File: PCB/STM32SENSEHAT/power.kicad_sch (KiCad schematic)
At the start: 30 parts, among them IC1 DW01A, J1 USB_B_Micro, J7 Conn_01x05_Pin, Q1 NMOS, Q2 NMOS, U1 MCP1700x-330xxTT, U2 TP4056, U3 FT230XQ

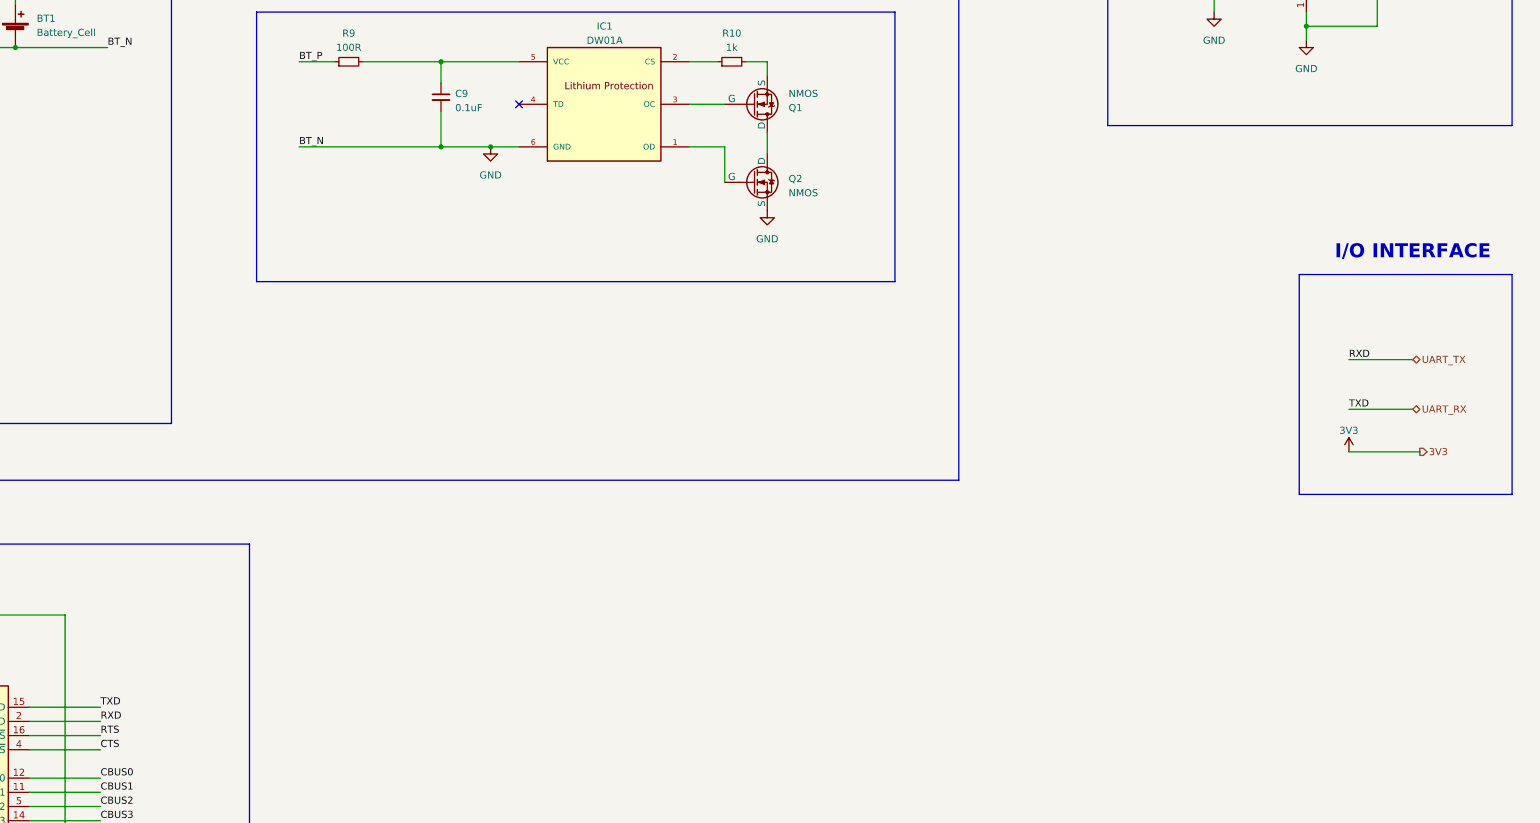
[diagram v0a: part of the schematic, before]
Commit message: Removed the extra sensor, Modified BME280 interfacing and FTDI UART pins. Added Manual Reset to MCU and configured BOOT pin
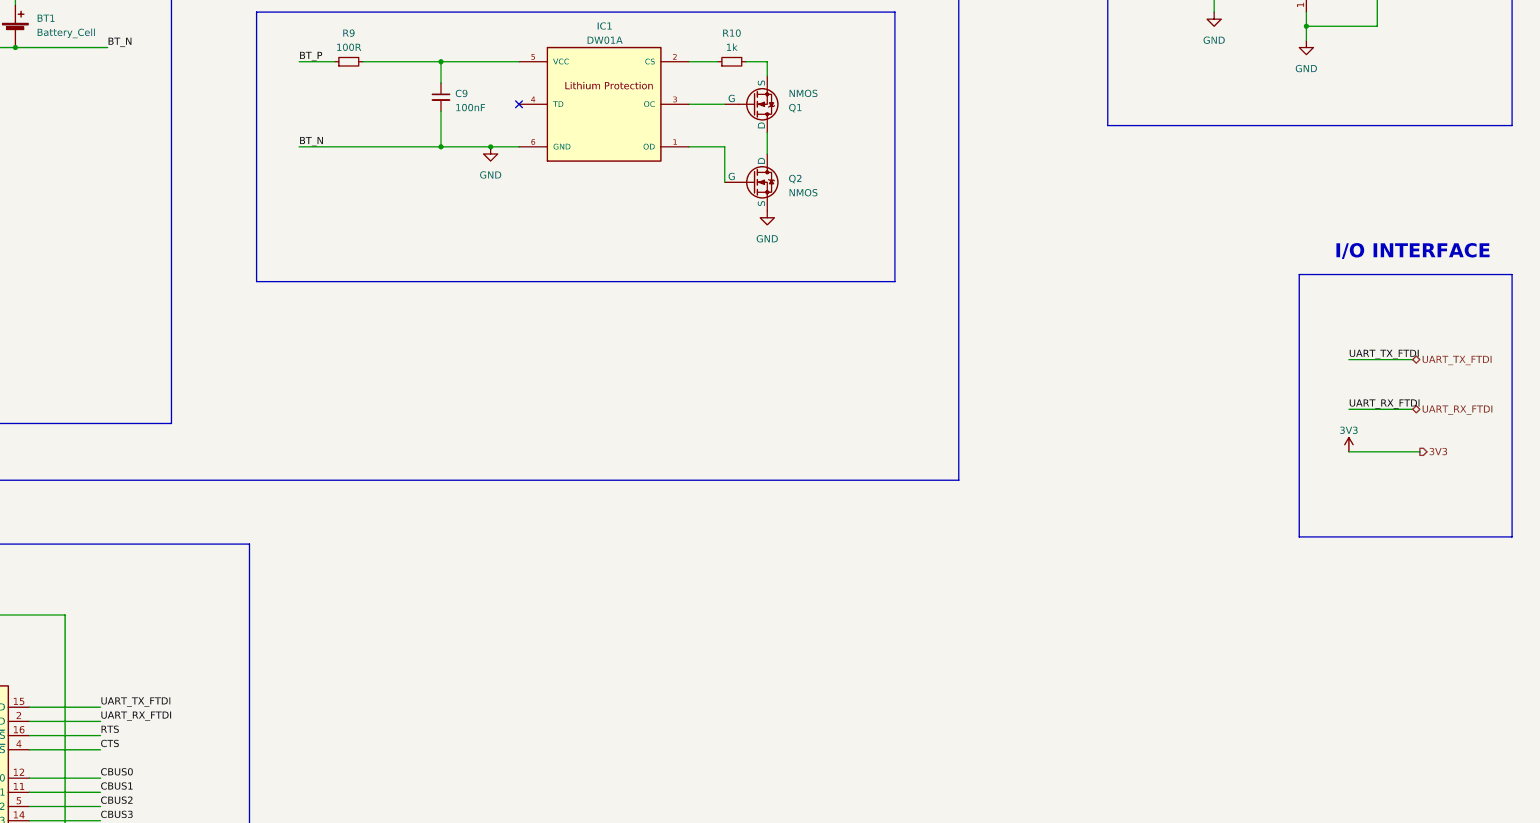
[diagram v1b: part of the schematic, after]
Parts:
- C9: value 0.1uF -> 100nF
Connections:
- net UART_RX renamed UART_TX_FTDI
- net UART_TX renamed UART_RX_FTDI
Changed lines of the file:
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@@
     (fill (type none))
   )
-  (rectangle (start 359.41 101.6) (end 397.51 140.97)
+  (rectangle (start 359.41 101.6) (end 397.51 148.59)
     (stroke (width 0) (type default))
     (fill (type none))
@@
     (effects (font (size 1.27 1.27)) (justify left bottom))
   )
-  (label "TXD" (at 368.3 125.73 0) (fields_autoplaced)
-    (effects (font (size 1.27 1.27)) (justify left bottom))
-  )
   (label "BT_N" (at 180.34 78.74 0) (fields_autoplaced)
     (effects (font (size 1.27 1.27)) (justify left bottom))
   )
+  (label "UART_RX_FTDI" (at 368.3 125.73 0) (fields_autoplaced)
+    (effects (font (size 1.27 1.27)) (justify left bottom))
+  )
   (label "D-" (at 50.8 189.23 0) (fields_autoplaced)
     (effects (font (size 1.27 1.27)) (justify left bottom))
@@
     (effects (font (size 1.27 1.27)) (justify left bottom))
   )
+  (label "UART_TX_FTDI" (at 144.78 179.07 0) (fields_autoplaced)
+    (effects (font (size 1.27 1.27)) (justify left bottom))
+  )
   (label "BT_P" (at 180.34 63.5 0) (fields_autoplaced)
     (effects (font (size 1.27 1.27)) (justify left bottom))
@@
     (effects (font (size 1.27 1.27)) (justify left bottom))
   )
-  (label "RXD" (at 144.78 181.61 0) (fields_autoplaced)
-    (effects (font (size 1.27 1.27)) (justify left bottom))
-  )
   (label "D-" (at 97.79 240.03 0) (fields_autoplaced)
     (effects (font (size 1.27 1.27)) (justify left bottom))
@@
     (effects (font (size 1.27 1.27)) (justify left bottom))
   )
+  (label "UART_RX_FTDI" (at 144.78 181.61 0) (fields_autoplaced)
+    (effects (font (size 1.27 1.27)) (justify left bottom))
+  )
   (label "BT_P" (at 335.28 46.99 0) (fields_autoplaced)
     (effects (font (size 1.27 1.27)) (justify left bottom))
@@
     (effects (font (size 1.27 1.27)) (justify left bottom))
   )
-  (label "TXD" (at 144.78 179.07 0) (fields_autoplaced)
+  (label "UART_TX_FTDI" (at 368.3 116.84 0) (fields_autoplaced)
     (effects (font (size 1.27 1.27)) (justify left bottom))
   )
@@
   )
   (label "VBUS" (at 50.8 181.61 0) (fields_autoplaced)
-    (effects (font (size 1.27 1.27)) (justify left bottom))
-  )
-  (label "RXD" (at 368.3 116.84 0) (fields_autoplaced)
     (effects (font (size 1.27 1.27)) (justify left bottom))
   )
@@
     (effects (font (size 1.27 1.27)) (justify left))
   )
-  (hierarchical_label "UART_TX" (shape bidirectional) (at 379.73 116.84 0) (fields_autoplaced)
+  (hierarchical_label "UART_TX_FTDI" (shape bidirectional) (at 379.73 116.84 0) (fields_autoplaced)
     (effects (font (size 1.27 1.27)) (justify left))
   )
-  (hierarchical_label "UART_RX" (shape bidirectional) (at 379.73 125.73 0) (fields_autoplaced)
+  (hierarchical_label "UART_RX_FTDI" (shape bidirectional) (at 379.73 125.73 0) (fields_autoplaced)
     (effects (font (size 1.27 1.27)) (justify left))
   )
@@
       (effects (font (size 1.27 1.27)) (justify left))
     )
-    (property "Value" "0.1uF" (at 208.28 71.7613 0)
-      (effects (font (size 1.27 1.27)) (justify left))
-    )
+    (property "Value" "100nF" (at 208.28 71.7613 0)
+      (effects (font (size 1.27 1.27)) (justify left))
+    )

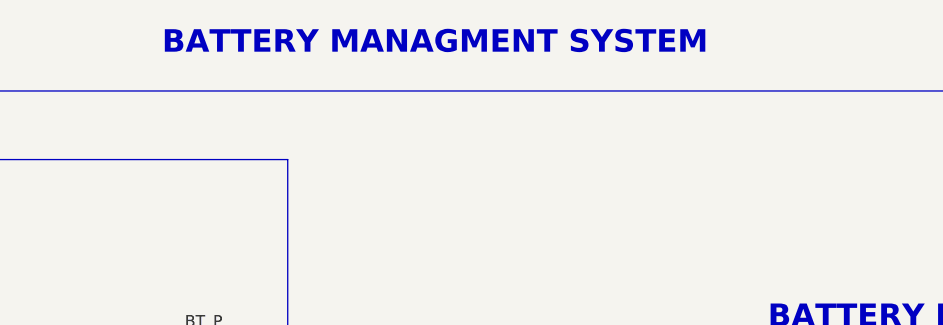
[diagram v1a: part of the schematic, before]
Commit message: Add STM32SENSEHAT, power, sensor, and mcu schematic file
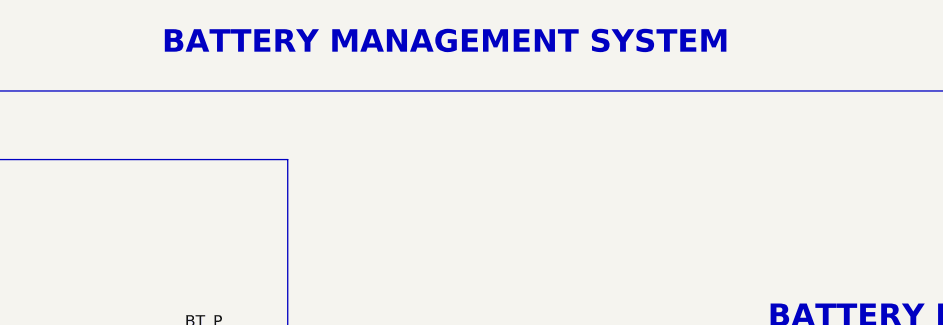
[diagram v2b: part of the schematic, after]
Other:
- note added: "BATTERY MANAGEMENT SYSTEM"
- note removed: "BATTERY MANAGMENT SYSTEM"
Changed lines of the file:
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@@
     (effects (font (size 2.5 2.5) (thickness 0.5) bold) (justify left bottom))
   )
-  (text "BATTERY MANAGMENT SYSTEM\n" (at 143.51 20.32 0)
+  (text "BATTERY MANAGEMENT SYSTEM\n" (at 143.51 20.32 0)
     (effects (font (size 2.5 2.5) (thickness 0.5) bold) (justify left bottom))
   )

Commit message: Revised schematics. Moved USB and EEPROM sub modules to MCU sheet and and rectified the top sheet accordingly
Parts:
- removed C1, C2: 47pF, symbol Device:C_Small
- removed C3: 10nF, symbol Device:C_Small
- removed C4, C5: 100nF, symbol Device:C_Small
- removed C6: 4.7uF, symbol Device:C_Small
- removed FB1: FerriteBead, symbol Device:FerriteBead
- removed J1: USB_B_Micro, symbol Connector:USB_B_Micro
- removed J7: Conn_01x05_Pin, symbol Connector:Conn_01x05_Pin
- removed R2, R3: 27R, symbol Device:R_Small
- removed U3: FT230XQ, Package_DFN_QFN:QFN-16-1EP_4x4mm_P0.65mm_EP2.1x2.1mm, symbol Interface_USB:FT230XQ
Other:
- note removed: "USB-FTDI INTERFACE"

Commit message: Added Battery Volatge Sesnsing capability
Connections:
- net BT_P renamed BAT_VOLTAGE
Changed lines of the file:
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@@
     (stroke (width 0) (type default))
   )
-  (wire (pts (xy 368.3 133.35) (xy 381 133.35))
+  (wire (pts (xy 350.52 123.19) (xy 363.22 123.19))
     (stroke (width 0) (type default))
   )
@@
     (stroke (width 0) (type default))
   )
+  (wire (pts (xy 350.52 107.95) (xy 363.22 107.95))
+    (stroke (width 0) (type default))
+  )
   (wire (pts (xy 82.55 104.14) (xy 82.55 96.52))
     (stroke (width 0) (type default))
@@
     (fill (type none))
   )
-  (rectangle (start 359.41 101.6) (end 397.51 148.59)
+  (rectangle (start 341.63 91.44) (end 379.73 138.43)
     (stroke (width 0) (type default))
     (fill (type none))
@@
     (effects (font (size 2.5 2.5) (thickness 0.5) bold) (justify left bottom))
   )
-  (text "I/O INTERFACE" (at 365.76 99.06 0)
+  (text "I/O INTERFACE" (at 347.98 88.9 0)
     (effects (font (size 2.5 2.5) (thickness 0.5) bold) (justify left bottom))
   )
@@
     (effects (font (size 1.27 1.27)) (justify left bottom))
   )
+  (label "BT_P" (at 350.52 107.95 0) (fields_autoplaced)
+    (effects (font (size 1.27 1.27)) (justify left bottom))
+  )
   (hierarchical_label "5V_USB" (shape input) (at 101.6 43.18 0) (fields_autoplaced)
     (effects (font (size 1.27 1.27)) (justify left))
   )
-  (hierarchical_label "3V3" (shape output) (at 381 133.35 0) (fields_autoplaced)
+  (hierarchical_label "3V3" (shape output) (at 363.22 123.19 0) (fields_autoplaced)
+    (effects (font (size 1.27 1.27)) (justify left))
+  )
+  (hierarchical_label "BAT_VOLTAGE" (shape input) (at 363.22 107.95 0) (fields_autoplaced)
     (effects (font (size 1.27 1.27)) (justify left))
   )
@@
     )
   )
-  (symbol (lib_id "power:VCC") (at 368.3 133.35 0) (unit 1)
-    (in_bom yes) (on_board yes) (dnp no) (fields_autoplaced)
-    (property "Reference" "#PWR052" (at 368.3 137.16 0)
-      (effects (font (size 1.27 1.27)) hide)
-    )
-    (property "Value" "3V3" (at 368.3 129.54 0)
+  (symbol (lib_id "power:VCC") (at 350.52 123.19 0) (unit 1)
+    (in_bom yes) (on_board yes) (dnp no) (fields_autoplaced)
+    (property "Reference" "#PWR052" (at 350.52 127 0)
+      (effects (font (size 1.27 1.27)) hide)
+    )
+    (property "Value" "3V3" (at 350.52 119.38 0)
       (effects (font (size 1.27 1.27) (color 132 0 0 1)))
     )
-    (property "Footprint" "" (at 368.3 133.35 0)
-      (effects (font (size 1.27 1.27)) hide)
-    )
-    (property "Datasheet" "" (at 368.3 133.35 0)
-      (effects (font (size 1.27 1.27)) hide)
-    )
+    (property "Footprint" "" (at 350.52 123.19 0)
+      (effects (font (size 1.27 1.27)) hide)
+    )
+    (property "Datasheet" "" (at 350.52 123.19 0)
+      (effects (font (size 1.27 1.27)) hide)
+    )

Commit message: Protectuion features added to all schematica
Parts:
- removed Q1, Q2: NMOS, symbol Simulation_SPICE:NMOS
- added C15, C16, C17: 1uF, symbol Device:C_Small
- added D3: D_Schottky, symbol Device:D_Schottky
- added Q1: AO3401A, Package_TO_SOT_SMD:SOT-23, symbol Transistor_FET:AO3401A
- added R19 (x4): 0R, symbol Device:R_Small
- added R35: 10k, symbol Device:R_Small
- added TP5, TP6: TestPoint, symbol Connector:TestPoint
- added U7: 8205A, TSSOP8, symbol 8205A:8205A
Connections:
- net BAT_VOLTAGE: now also Q1.3 (D); no longer C10.1, U1.3 (VI)
- net GND: now also C15.2, C16.2, C17.2, R19.1, R19.2, R35.2
- net VCC: no longer C11.1, U1.2 (VO), U2.4 (VCC), U2.8 (CE)
- net OD: now reaches IC1.1 (OD)
- net OD: now also U7.4 (G1)
- net S2: now reaches R10.2
- net S2: now also R19.1, R19.2
- net OC: now reaches IC1.3 (OC)
- net OC: now also U7.5 (G2)
- new net: U7.1 (D1), U7.8 (D2)
- new net: R19.2, U7.2 (S1)
- new net: R19.1, U7.3 (S1_2)
- new net: R19.2, U7.6 (S2_2)
- new net: R19.1, U7.7 (S2)
- new net: D3.2 (A), Q1.1 (G)
- new net 3V3: C11.1, C15.1, C16.1, C17.1, TP6.1, U1.2 (VO)
- new net 5VUSB: R35.1, TP5.1, U2.4 (VCC), U2.8 (CE)
- new net LOAD_PWR: C10.1, D3.1 (K), Q1.2 (S), U1.3 (VI)
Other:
- moved on the sheet: BT1, C10, C11, C7, C8, C9, D1, D2, IC1, R10, R4, R5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

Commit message: Schematics reviewed
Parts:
- D1, D2: footprint (none) -> LED_THT:LED_D5.0mm
- IC1: footprint SOT23-6 -> DW01A:SOT23-6
- TP5, TP6: footprint (none) -> TestPoint:TestPoint_Pad_D3.0mm
- U2: footprint SOP127P600X175-9N -> TP4056:SOP127P600X175-9N
- U7: footprint TSSOP8 -> 8205A:TSSOP8
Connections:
- net VCC is gone; now on net 5VUSB: R4.1
- net 5VUSB: now also D3.2 (A), Q1.1 (G)
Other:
- note removed: "I/O INTERFACE"

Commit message: Added footprints to the components but still pending review by Rumbizdai and Phomolo
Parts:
- BT1: footprint (none) -> Battery:BatteryHolder_Keystone_1042_1x18650
- C10, C11, C15, C16, C17, C7, C8, C9: footprint (none) -> Capacitor_SMD:C_0805_2012Metric
- D3: footprint (none) -> Package_TO_SOT_SMD:TSOT-23-6
- R10, R5: footprint (none) -> Resistor_SMD:R_0603_1608Metric
- R19, R35, R4, R6, R9: footprint (none) -> Resistor_SMD:R_0805_2012Metric
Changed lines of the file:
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@@
       (effects (font (size 1.27 1.27)) (justify left))
     )
-    (property "Footprint" "" (at 76.2 139.7 0)
+    (property "Footprint" "Capacitor_SMD:C_0805_2012Metric" (at 76.2 139.7 0)
       (effects (font (size 1.27 1.27)) hide)
     )
@@
       (effects (font (size 1.27 1.27)) (justify left))
     )
-    (property "Footprint" "" (at 328.93 88.9 0)
+    (property "Footprint" "Capacitor_SMD:C_0805_2012Metric" (at 328.93 88.9 0)
       (effects (font (size 1.27 1.27)) hide)
     )
@@
       (effects (font (size 1.27 1.27)) (justify left))
     )
-    (property "Footprint" "" (at 76.2 124.46 0)
+    (property "Footprint" "Resistor_SMD:R_0603_1608Metric" (at 76.2 124.46 0)
       (effects (font (size 1.27 1.27)) hide)
     )
@@
       (effects (font (size 1.27 1.27)) (justify left))
     )
-    (property "Footprint" "" (at 320.04 88.9 0)
+    (property "Footprint" "Capacitor_SMD:C_0805_2012Metric" (at 320.04 88.9 0)
       (effects (font (size 1.27 1.27)) hide)
     )
@@
       (effects (font (size 1.27 1.27)))
     )
-    (property "Footprint" "" (at 40.64 199.39 0)
+    (property "Footprint" "Resistor_SMD:R_0805_2012Metric" (at 40.64 199.39 0)
       (effects (font (size 1.27 1.27)) hide)
     )
@@
       (effects (font (size 1.27 1.27)) (justify left))
     )
-    (property "Footprint" "" (at 40.64 85.09 0)
+    (property "Footprint" "Resistor_SMD:R_0805_2012Metric" (at 40.64 85.09 0)
       (effects (font (size 1.27 1.27)) hide)
     )
@@
       (effects (font (size 1.27 1.27)) (justify left))
     )
-    (property "Footprint" "" (at 337.82 88.9 0)
+    (property "Footprint" "Capacitor_SMD:C_0805_2012Metric" (at 337.82 88.9 0)
       (effects (font (size 1.27 1.27)) hide)
     )
@@
       (effects (font (size 1.27 1.27)) (justify left))
     )
-    (property "Footprint" "" (at 121.92 64.77 0)
+    (property "Footprint" "Resistor_SMD:R_0805_2012Metric" (at 121.92 64.77 0)
       (effects (font (size 1.27 1.27)) hide)
     )
@@
       (effects (font (size 1.27 1.27)) (justify left))
     )
-    (property "Footprint" "" (at 58.42 99.06 0)
+    (property "Footprint" "Resistor_SMD:R_0805_2012Metric" (at 58.42 99.06 0)
       (effects (font (size 1.27 1.27)) hide)
     )
@@
       (effects (font (size 1.27 1.27)) (justify left))
     )
-    (property "Footprint" "" (at 130.81 77.216 90)
+    (property "Footprint" "Battery:BatteryHolder_Keystone_1042_1x18650" (at 130.81 77.216 90)
       (effects (font (size 1.27 1.27)) hide)
     )
@@
       (effects (font (size 1.27 1.27)) (justify left))
     )
-    (property "Footprint" "" (at 311.15 88.9 0)
+    (property "Footprint" "Capacitor_SMD:C_0805_2012Metric" (at 311.15 88.9 0)
       (effects (font (size 1.27 1.27)) hide)
     )
@@
       (effects (font (size 1.27 1.27)))
     )
-    (property "Footprint" "" (at 149.86 228.6 0)
+    (property "Footprint" "Resistor_SMD:R_0805_2012Metric" (at 149.86 228.6 0)
       (effects (font (size 1.27 1.27)) hide)
     )
@@
       (effects (font (size 1.27 1.27)))
     )
-    (property "Footprint" "" (at 109.22 199.39 0)
+    (property "Footprint" "Resistor_SMD:R_0603_1608Metric" (at 109.22 199.39 0)
       (effects (font (size 1.27 1.27)) hide)
     )
@@
       (effects (font (size 1.27 1.27)))
     )
-    (property "Footprint" "" (at 187.96 229.87 0)
+    (property "Footprint" "Resistor_SMD:R_0805_2012Metric" (at 187.96 229.87 0)
       (effects (font (size 1.27 1.27)) hide)
     )
@@
       (effects (font (size 1.27 1.27)))
     )
-    (property "Footprint" "" (at 152.4 228.6 0)
+    (property "Footprint" "Resistor_SMD:R_0805_2012Metric" (at 152.4 228.6 0)
       (effects (font (size 1.27 1.27)) hide)
     )
@@
       (effects (font (size 1.27 1.27)))
     )
-    (property "Footprint" "" (at 190.5 229.87 0)
+    (property "Footprint" "Resistor_SMD:R_0805_2012Metric" (at 190.5 229.87 0)
       (effects (font (size 1.27 1.27)) hide)
     )
@@
       (effects (font (size 1.27 1.27)) (justify left))
     )
-    (property "Footprint" "" (at 111.76 74.93 0)
+    (property "Footprint" "Capacitor_SMD:C_0805_2012Metric" (at 111.76 74.93 0)
       (effects (font (size 1.27 1.27)) hide)
     )
@@
       (effects (font (size 1.27 1.27)) (justify right))
     )
-    (property "Footprint" "" (at 163.83 64.77 0)
+    (property "Footprint" "Package_TO_SOT_SMD:TSOT-23-6" (at 163.83 64.77 0)
       (effects (font (size 1.27 1.27)) hide)
     )
@@
       (effects (font (size 1.27 1.27)) (justify left))
     )
-    (property "Footprint" "" (at 281.94 86.36 0)
+    (property "Footprint" "Capacitor_SMD:C_0805_2012Metric" (at 281.94 86.36 0)
       (effects (font (size 1.27 1.27)) hide)
     )
@@
       (effects (font (size 1.27 1.27)) (justify left))
     )
-    (property "Footprint" "" (at 57.15 205.74 0)
-      (effects (font (size 1.27 1.27)) hide)
-    )
+    (property "Footprint" "Capacitor_SMD:C_0805_2012Metric" (at 57.15 205.74 0)
+      (effects (font (size 1.27 1.27)) hide)
+    )
